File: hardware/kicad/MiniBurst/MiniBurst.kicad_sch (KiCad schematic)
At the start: 73 parts, among them J1 TRIG_IN, J2 TRIG_OUT, J3 EXT_CLK, J4 DURATION_OUT, J5 END_OUT, J6 PULSES_OUT, J8 Conn_01x10_Pin, SW1 RETRIG, SW2 STEPS, U1 LM358, U2 40106, U3 4017, U4 LM358, U5 LM358

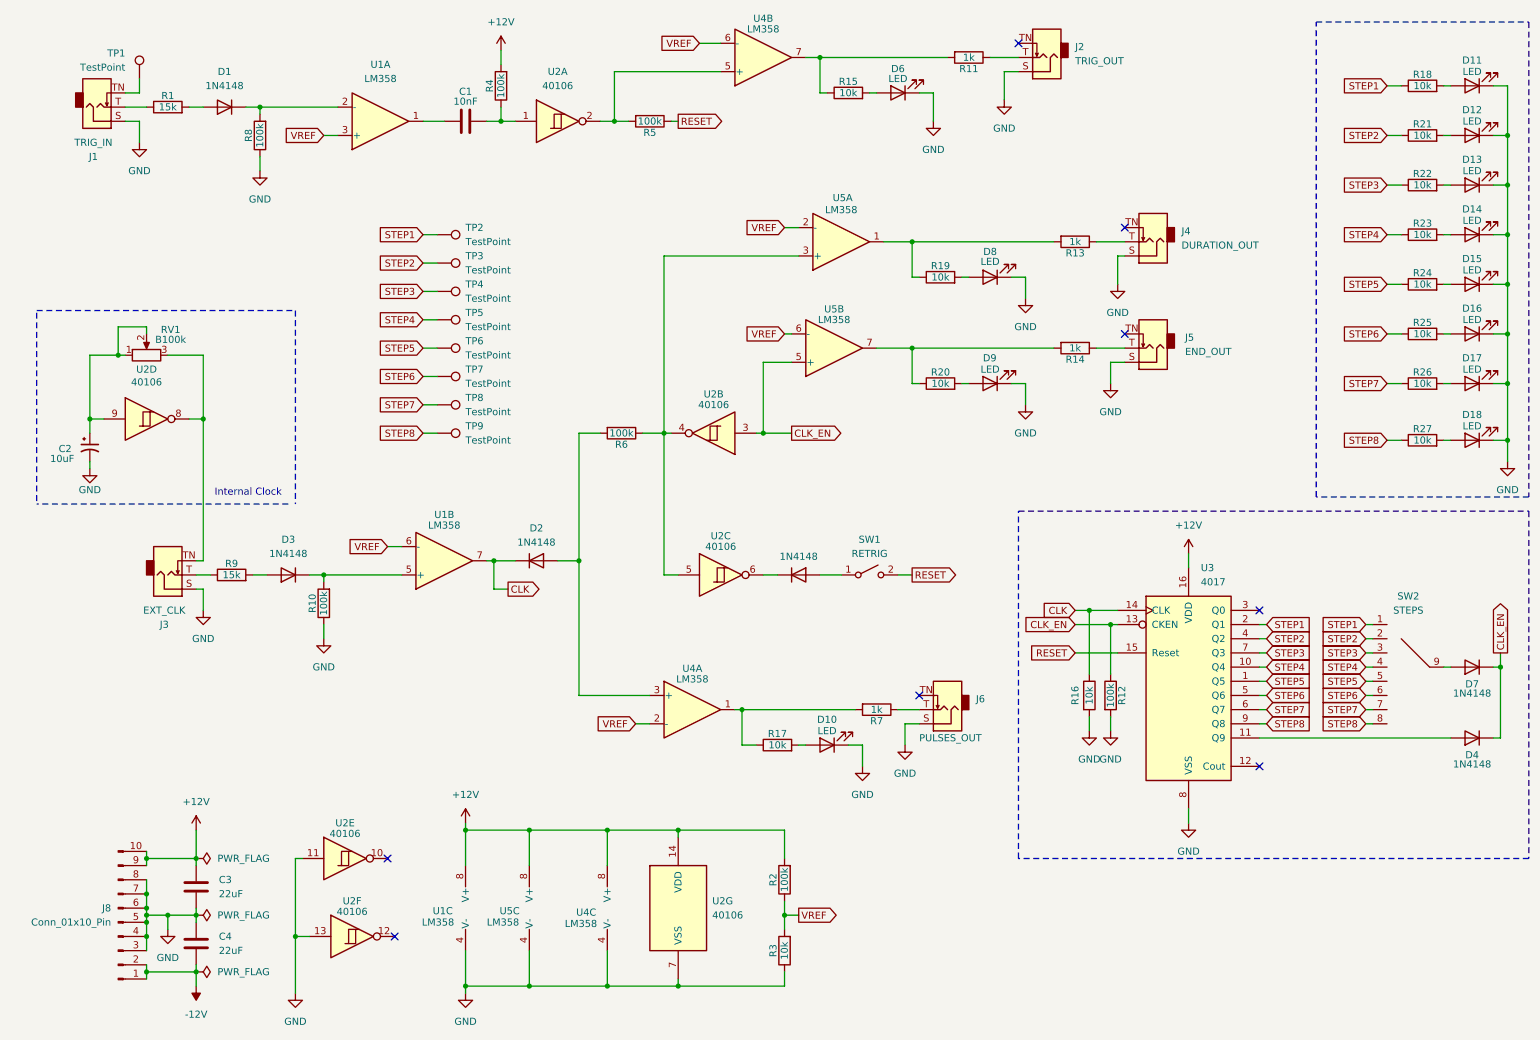
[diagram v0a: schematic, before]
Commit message: done with panel art
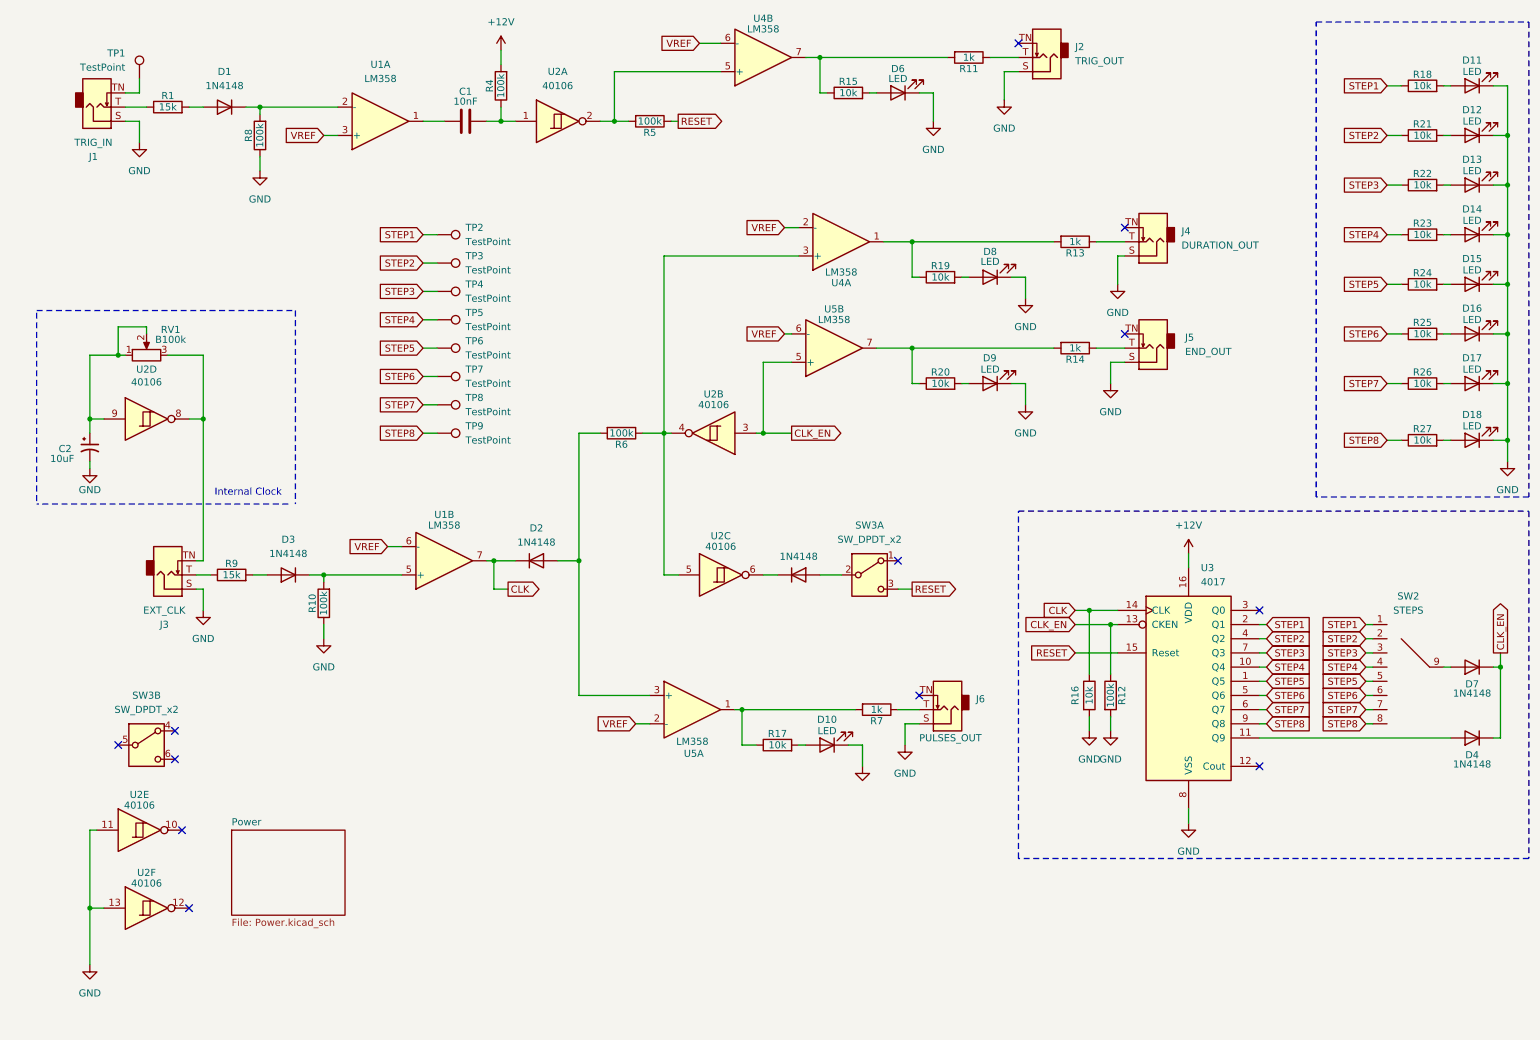
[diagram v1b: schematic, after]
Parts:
- removed C3, C4: 22uF, Capacitor_SMD:CP_Elec_6.3x4.5, symbol Device:C
- removed J8: Conn_01x10_Pin, Connector_IDC:IDC-Header_2x05_P2.54mm_Vertical, symbol Connector:Conn_01x10_Pin
- removed R2: 100k, Resistor_SMD:R_0805_2012Metric, symbol Device:R
- removed R3: 10k, Resistor_SMD:R_0805_2012Metric, symbol Device:R
- removed SW1: RETRIG, benjiaomodular:ToggleSwitch_SMTS-102, symbol Switch:SW_SPST
- removed unit 3 of U1
- removed unit 7 of U2
- removed unit 3 of U4
- removed unit 3 of U5
- added SW3: SW_DPDT_x2, benjiaomodular:Button_KFC7x7, symbol Switch:SW_DPDT_x2
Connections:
- net RESET: now also SW3.3 (C)
- net at D5.2 (A): now also SW3.2 (B)
- net at R6.1, U2.4, U2.5: now also U4.3 (+); no longer U5.3 (+)
- net at R17.1, R7.2: now also U5.1; no longer U4.1
- net at D2.2 (A), R6.2: now also U5.3 (+); no longer U4.3 (+)
- net at R13.2, R19.1: now also U4.1; no longer U5.1
- no-connect marks 8 -> 12
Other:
- added sheet Power (Power.kicad_sch)
- company: (none) -> benjiaomodular
- title: (none) -> MiniBurst
- moved on the sheet: U2E, U2F, U4A, U5A

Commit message: v0.1 PCB
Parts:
- removed TP2, TP3, TP4, TP5, TP6, TP7, TP8, TP9: TestPoint, Connector_Wire:SolderWirePad_1x01_SMD_1x2mm, symbol Connector:TestPoint
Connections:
- net CLK_EN: now also U2.5; no longer U2.3
- net at D5.1 (K): now also U2.4; no longer U2.6
- net at R6.1, U4.3 (+): now also U2.3, U2.6; no longer U2.4, U2.5
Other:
- moved on the sheet: U2B, U2C
